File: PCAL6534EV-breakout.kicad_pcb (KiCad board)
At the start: 6 copper layers, 15.2 x 50.8 mm, 16 parts, among them J1 SM04B-SRSS-TB, J2 Conn_01x20, J3 Conn_01x20, J4 Conn_02x04_Odd_Even, U1 PCAL6534EV

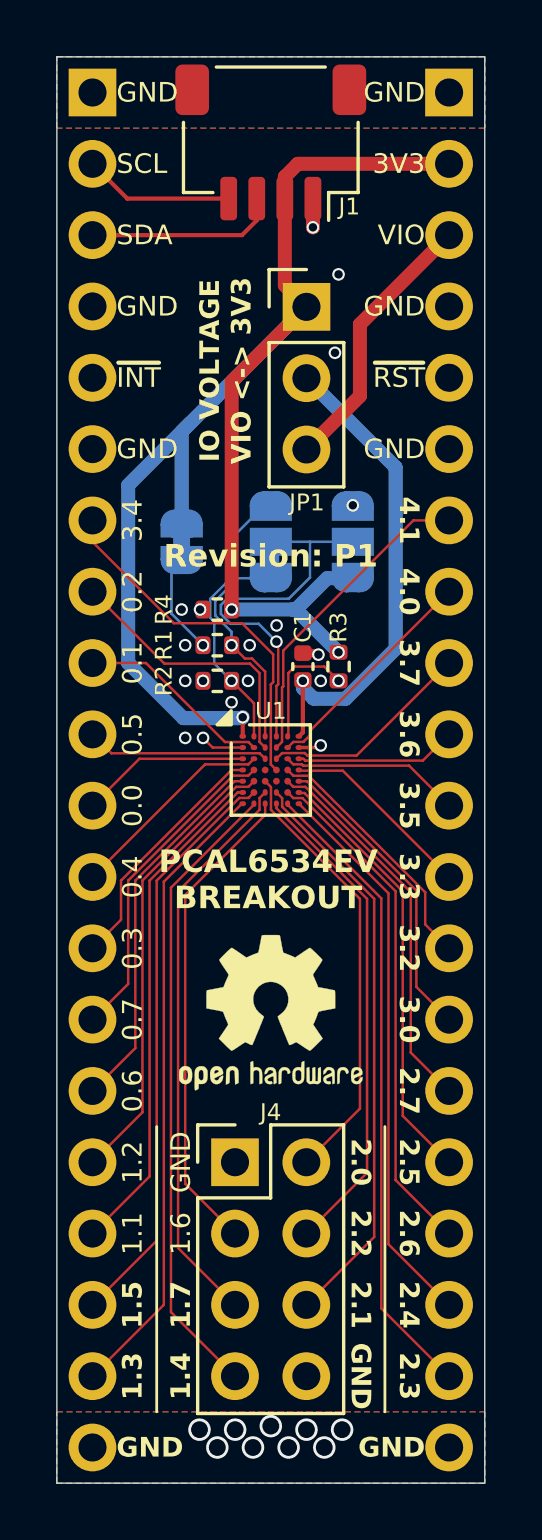
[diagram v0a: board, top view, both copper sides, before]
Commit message: add fiducials; add pilot hole for drilling a mounting hole
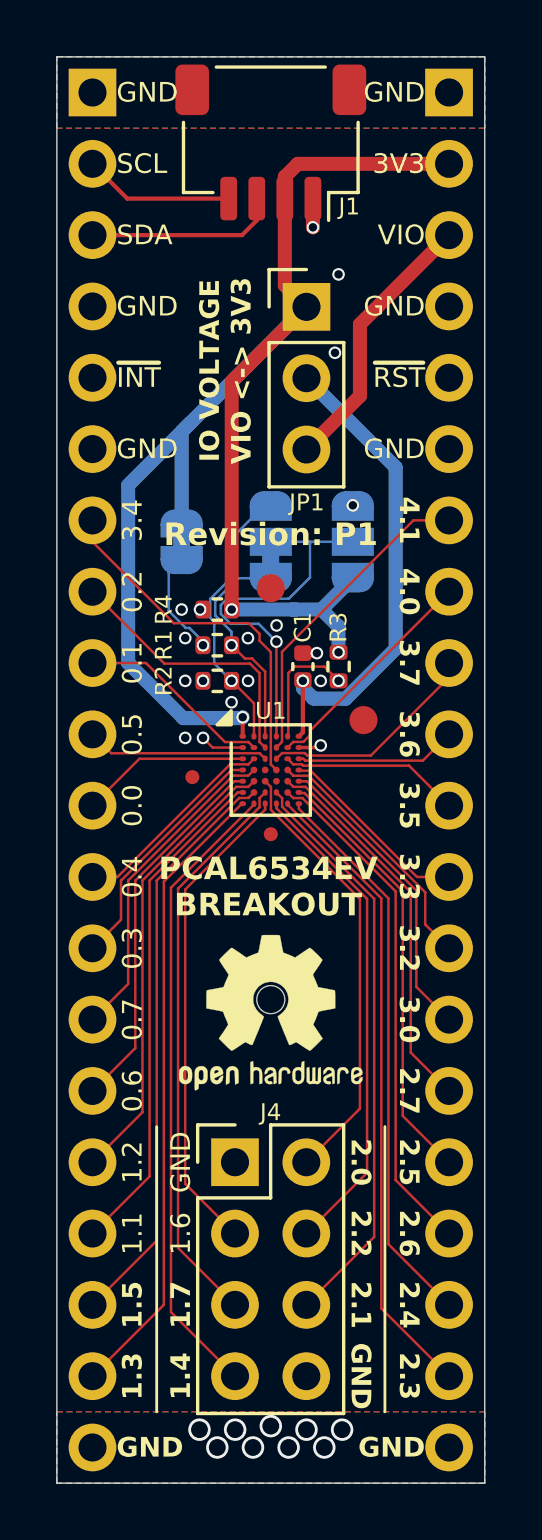
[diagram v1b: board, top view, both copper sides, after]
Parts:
- added ?: , , F.Cu at (158.3, 108.7)
- added ?: , , F.Cu at (155.0, 104.0)
- added REF**: Fiducial_0.5mm_Mask1mm, Fiducial:Fiducial_0.5mm_Mask1mm, F.Cu at (152.2, 110.7)
- added REF**: TestPoint_THTPad_D1.0mm_Drill0.5mm, TestPoint:TestPoint_THTPad_D1.0mm_Drill0.5mm, F.Cu at (155.0, 118.7)
- added REF**: Fiducial_0.5mm_Mask1mm, Fiducial:Fiducial_0.5mm_Mask1mm, F.Cu at (155.0, 112.8)
- moved REF** 0.38 mm to (156.7, 116.3)

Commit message: nudge here, prod there, and pretty soon you've changed the entire thing
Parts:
- removed ? (x2): , 
- added FID3: Fiducial_1mm_Mask2mm, Fiducial:Fiducial_1mm_Mask2mm, F.Cu at (155.0, 103.9)
- added FID4: Fiducial_1mm_Mask2mm, Fiducial:Fiducial_1mm_Mask2mm, F.Cu at (158.2, 108.8)
- moved FID1 0.25 mm to (152.2, 110.5)
- renumbered REF** to FID1, REF** to FID2

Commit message: just slam them all in an update again
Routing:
- net P3_4: track 13.2 -> 12.4 mm
- net P0_5: track 6.51 -> 5.97 mm
- net P3_7: track 7.93 -> 7.42 mm
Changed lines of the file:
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@@
-	)
-	(segment
-		(start 149.031 109.591)
-		(end 148.65 109.21)
-		(width 0.09)
-		(layer "F.Cu")
-		(net 5)
 	)
 	(segment
@@
 	)
 	(segment
-		(start 154.4 111.68)
-		(end 154.4 111.715)
-		(width 0.09)
-		(layer "F.Cu")
-		(net 9)
-	)
-	(segment
 		(start 154.4 111.715)
 		(end 151.444 114.671)
@@
 	)
 	(segment
-		(start 148.65 102.353117)
-		(end 148.65 101.59)
-		(width 0.09)
-		(layer "F.Cu")
-		(net 10)
-	)
-	(segment
 		(start 155 110.28)
 		(end 155 106.27894)
@@
 	)
 	(segment
-		(start 155.6 111.68)
-		(end 155.6 111.731214)
-		(width 0.09)
-		(layer "F.Cu")
-		(net 11)
-	)
-	(segment
 		(start 159.096 115.227214)
 		(end 159.095997 129.815997)
@@
 	)
 	(segment
-		(start 161.35 107.178)
-		(end 161.35 106.67)
-		(width 0.09)
-		(layer "F.Cu")
-		(net 17)
-	)
-	(segment
 		(start 156.025 110.505)
 		(end 156.422 110.505)
@@
 	)
 	(segment
-		(start 156 110.48)
-		(end 156.025 110.505)
-		(width 0.09)
-		(layer "F.Cu")
-		(net 18)
-	)
-	(segment
 		(start 155.6 109.68)
 		(end 155.8 109.48)
@@
 		(layer "F.Cu")
 		(net 28)
-	)
-	(segment
-		(start 154 111.68)
-		(end 153.97 111.68)
-		(width 0.09)
-		(layer "F.Cu")
-		(net 29)
 	)
 	(segment
@@
 	)
 	(segment
-		(start 153.607 104.762988)
-		(end 153.607 104.765)
-		(width 0.5)
-		(layer "B.Cu")
-		(net 34)
-	)
-	(segment
 		(start 157.413 106.289)
 		(end 157.413 105.37)
@@
 	)
 	(segment
-		(start 154.78 101.052)
-		(end 155 101.052)
-		(width 0.09)
-		(layer "B.Cu")
-		(net 35)
-	)
-	(segment
 		(start 153.603 107.305)
 		(end 152.989002 106.691002)
@@
 	)
 	(segment
-		(start 156.01 109.27)
-		(end 156 109.27)
-		(width 0.15)
-		(layer "F.Cu")
-		(net 37)
-	)
-	(segment
 		(start 156.143 109.137)
 		(end 156.01 109.27)
@@
 	)
 	(segment
-		(start 157.394 107.235)
-		(end 157.413 107.305)
-		(width 0.09)
-		(layer "F.Cu")
-		(net 41)
-	)
-	(segment
 		(start 156.905 106.797)
 		(end 155.855106 106.797)
@@
 		(width 0.09)
 		(layer "F.Cu")
-		(net 41)
-	)
-	(segment
-		(start 155.624998 109.255002)
-		(end 155.6 109.28)
-		(width 0.09)
-		(layer "F.Cu")
